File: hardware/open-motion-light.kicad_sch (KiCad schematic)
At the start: 89 parts, among them J1 TYPE-C-31-M-12, J2 Conn_01x04, Q1 2N7002, SW1 SW_Push, SW2 SW_Push, SW3 SSSS213800, U1 CN3058E, U2 STM32L031G6U6, U3 MT9284BS6, U4 PIR223D-S0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

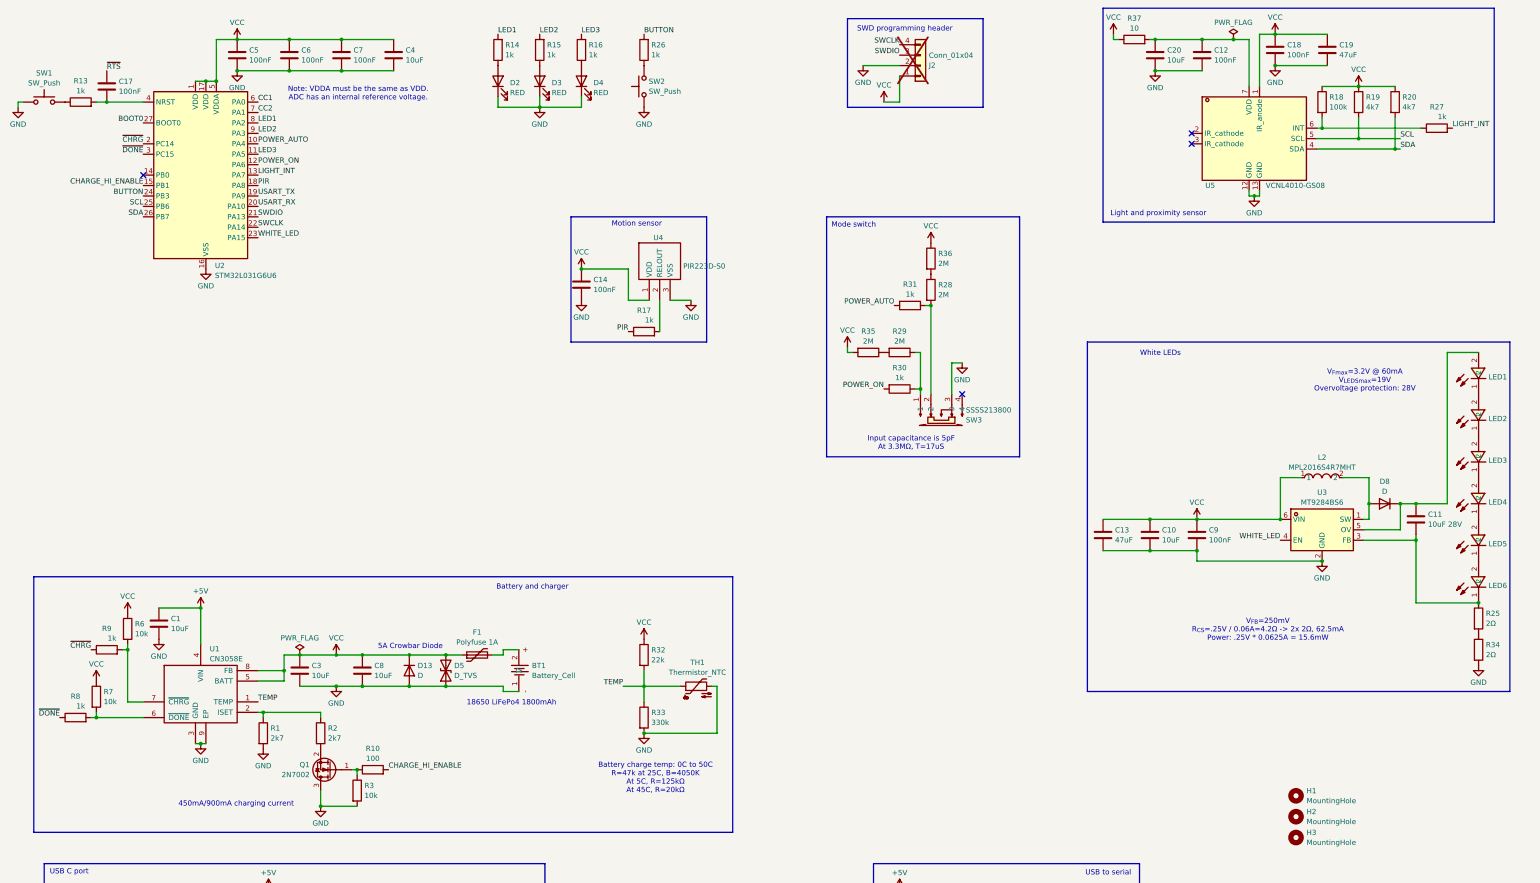
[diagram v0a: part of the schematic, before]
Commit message: Update schematic for v1.1
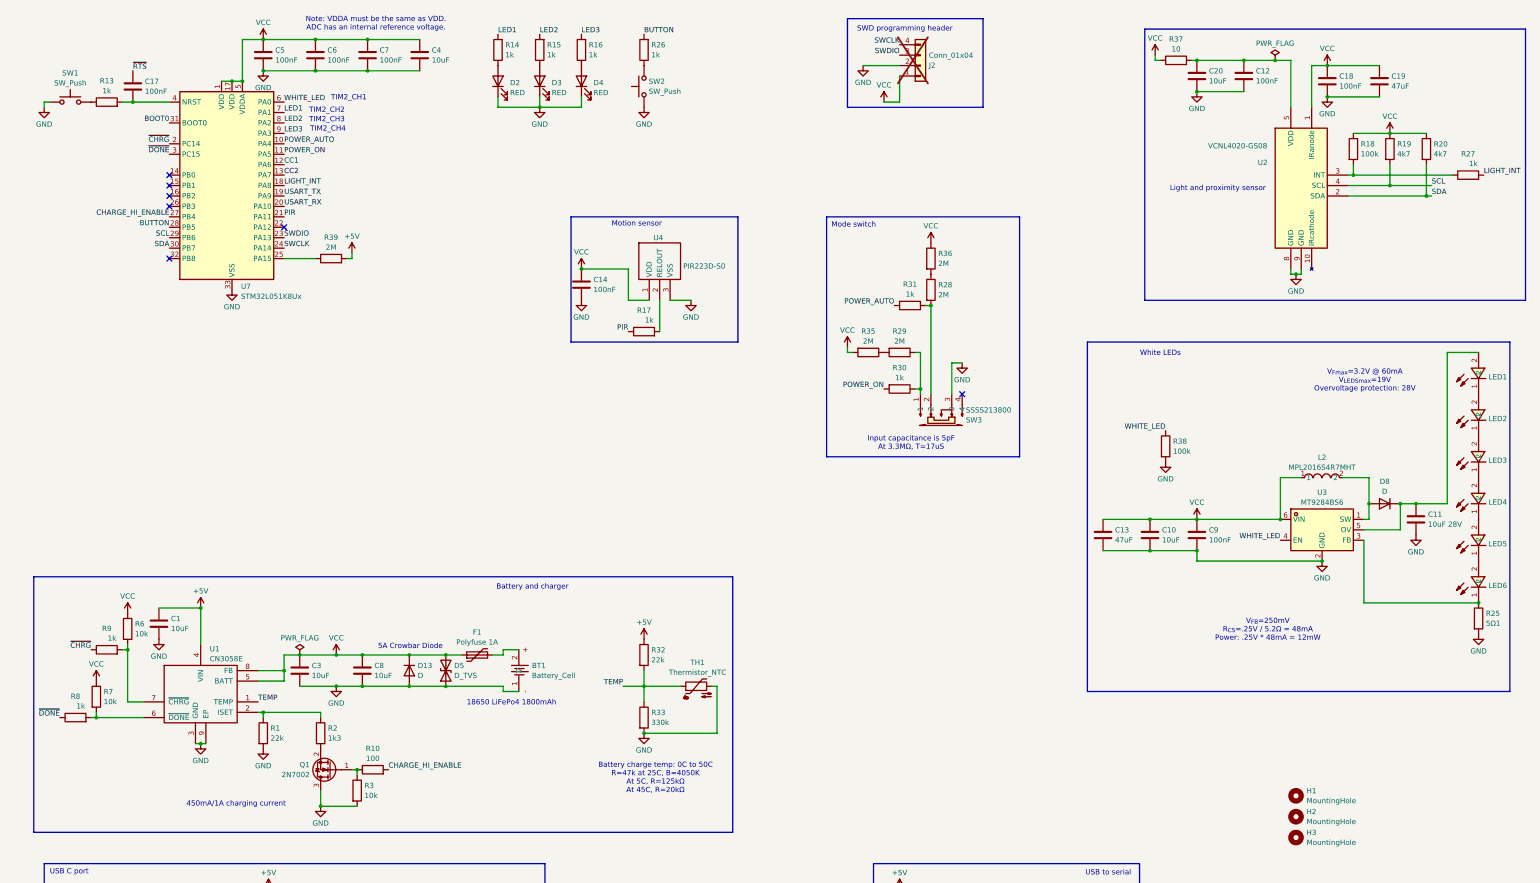
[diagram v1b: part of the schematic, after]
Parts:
- removed R34: 2Ω, Resistor_SMD:R_0603_1608Metric, symbol Device:R
- removed U2: STM32L031G6U6, Package_DFN_QFN:QFN-28_4x4mm_P0.5mm, symbol MCU_ST_STM32L0:STM32L031G6Ux
- removed U5: VCNL4010-GS08, Homebrew:SENSORS-SMD_VCNL4010-GS08, symbol Homebrew:VCNL4010-GS08
- added R38: 100k, Resistor_SMD:R_0402_1005Metric, symbol Device:R
- added R39: 2M, Resistor_SMD:R_0603_1608Metric, symbol Device:R
- added U2: VCNL4020-GS08, Homebrew:SENSOR-SMD_VCNL4020-GS08, symbol Homebrew:VCNL4020-GS08
- added U7: STM32L051K8Ux, Package_DFN_QFN:QFN-32-1EP_5x5mm_P0.5mm_EP3.45x3.45mm, symbol MCU_ST_STM32L0:STM32L051K8Ux
- R1: value 2k7 -> 22k; LCSC C13167 -> (none)
- R2: value 2k7 -> 1k3; LCSC C13167 -> (none)
- R25: value 2Ω -> 5Ω1; LCSC C22977 -> C25197
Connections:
- net +5V: now also R32.1, R39.2
- net BOOT0: now also U7.31 (BOOT0)
- net BUTTON: now also U7.28 (PB5)
- net CC1: now also U7.12 (PA6)
- net CC2: now also U7.13 (PA7)
- net CHARGE_HI_ENABLE: now also U7.27 (PB4)
- net GND: now also C11.2, R25.2, R38.2, U2.8 (GND), U2.9 (GND), U7.33 (VSS)
- net LED1: now also U7.7 (PA1)
- net LED2: now also U7.8 (PA2)
- net LED3: now also U7.9 (PA3)
- net LIGHT_INT: now also U7.18 (PA8)
- net PIR: now also U7.21 (PA11)
- net POWER_AUTO: now also U7.10 (PA4)
- net POWER_ON: now also U7.11 (PA5)
- net SCL: now also U2.4 (SCL), U7.29 (PB6)
- net SDA: now also U2.2 (SDA), U7.30 (PB7)
- net SWCLK: now also U7.24 (PA14)
- net SWDIO: now also U7.23 (PA13)
- net USART_RX: now also U7.20 (PA10)
- net USART_TX: now also U7.19 (PA9)
- net VCC: now also U2.1 (IRanode), U7.1 (VDD), U7.17 (VDD), U7.5 (VDDA); no longer R32.1
- net WHITE_LED: now also R38.1, U7.6 (PA0)
- net ~{CHRG}: now also U7.2 (PC14)
- net ~{DONE}: now also U7.3 (PC15)
- net at C12.2, C20.1, R37.2: now also U2.5 (VDD)
- net at C17.2, R13.2: now also U7.4 (NRST)
- net at R18.2, R27.1: now also U2.3 (INT)
- net at LED6.1, R25.1, U3.3 (FB): no longer C11.2
- new net: R39.1, U7.25 (PA15)
- no-connect marks 8 -> 11
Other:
- note added: "450mA/1A charging current"
- note added: "TIM2_CH1"
- note added: "TIM2_CH2"
- note added: "TIM2_CH3"
- note added: "TIM2_CH4"
- note added: "V_{FB}=250mV R_{CS}=.25V / 5.2Ω = 48mA Power: .25V * 48mA = 12mW"
- note removed: "450mA/900mA charging current"
- note removed: "V_{FB}=250mV R_{CS}=.25V / 0.06A=4.2Ω -> 2x 2Ω, 62.5mA Power: .25V * 0.0625A = 15.6mW"
- moved on the sheet: C12, C17, C18, C19, C20, C4, C5, C6, C7, R13, R18, R19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

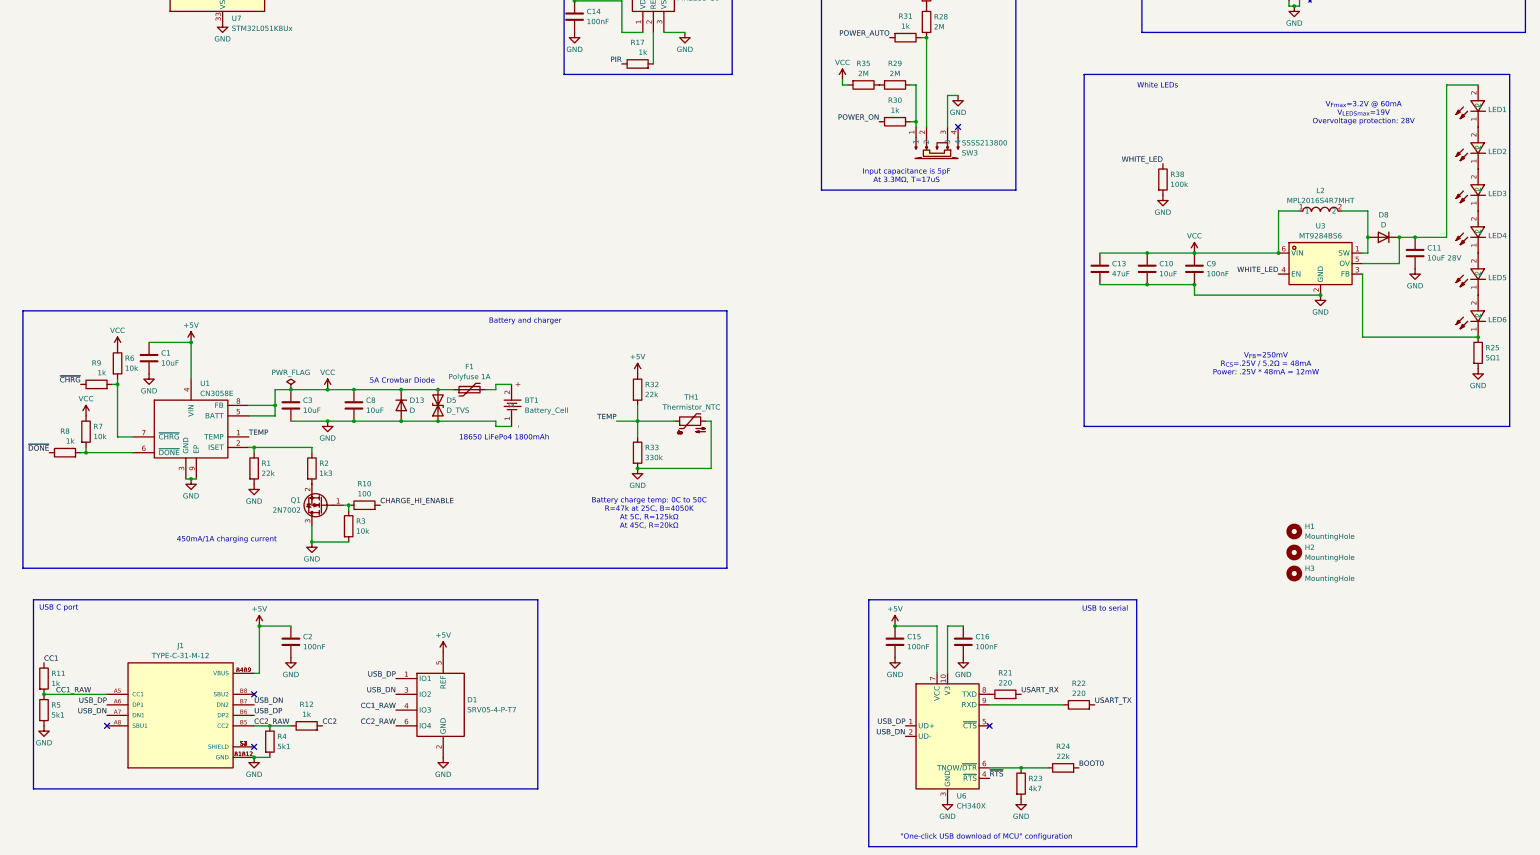
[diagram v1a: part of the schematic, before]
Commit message: More v1.1 schematic updates
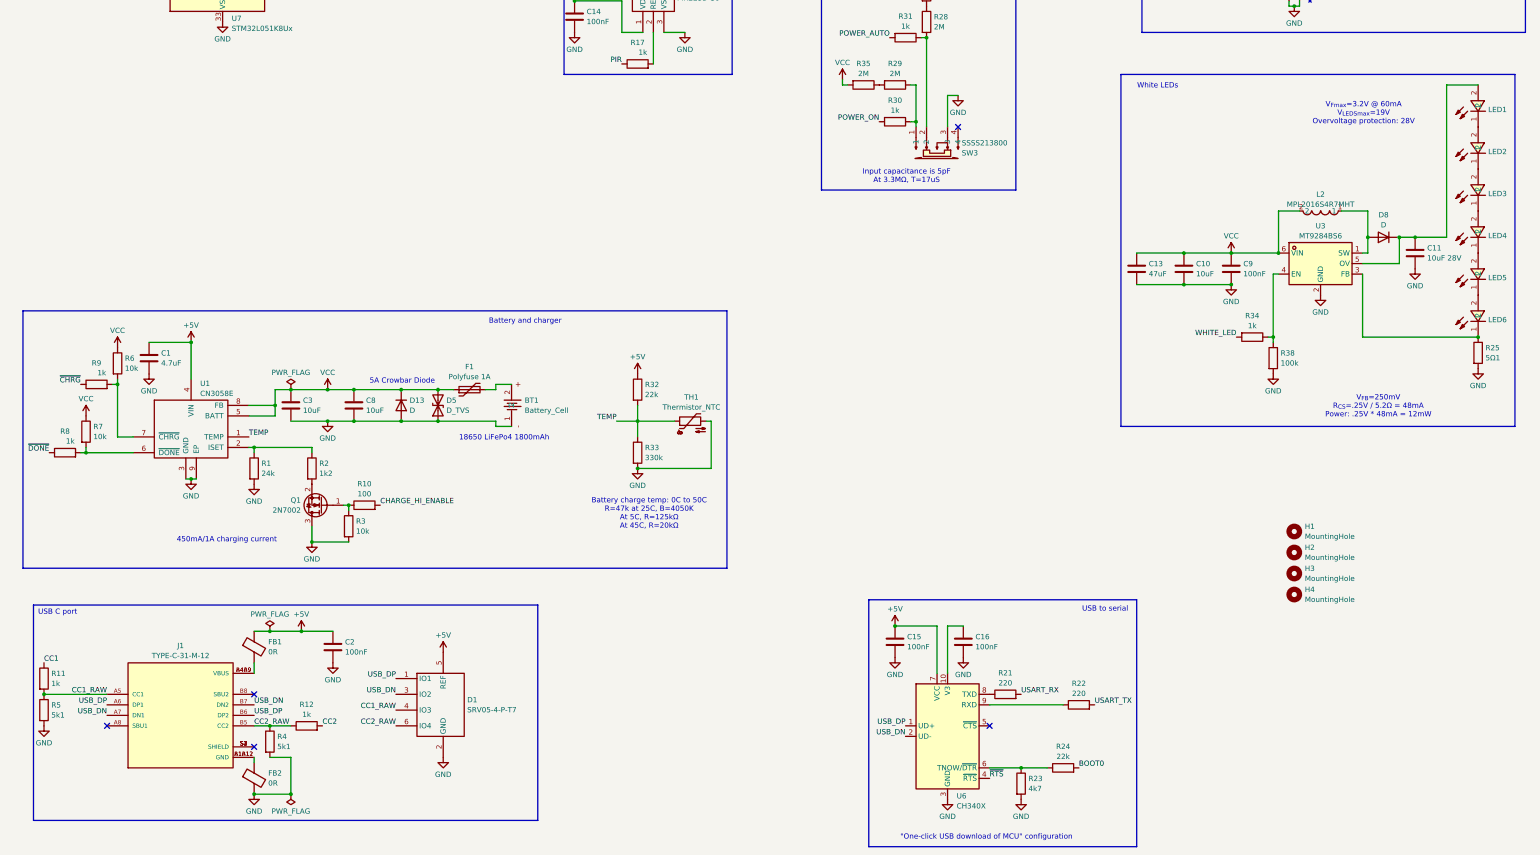
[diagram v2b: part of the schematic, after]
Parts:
- added FB1, FB2: 0R, Inductor_SMD:L_1206_3216Metric, symbol Device:FerriteBead
- added H4: MountingHole, MountingHole:MountingHole_3.2mm_M3_ISO7380, symbol Mechanical:MountingHole
- added R34: 1k, Resistor_SMD:R_0402_1005Metric, symbol Device:R
- C1: value 10uF -> 4.7uF; LCSC C96446 -> C19666
- R1: value 22k -> 24k; LCSC (none) -> C23352
- R2: value 1k3 -> 1k2; LCSC (none) -> 0603
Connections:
- net +5V: now also FB1.1; no longer J1.A4B9 (VBUS), J1.B4A9 (VBUS)
- net GND: now also FB2.2; no longer J1.A1B12 (GND), J1.B1A12 (GND)
- net VCC: now also L2.2; no longer L2.1
- net WHITE_LED: now also R34.2; no longer R38.1, U3.4 (EN)
- net at D8.2 (A), U3.1 (SW): now also L2.1; no longer L2.2
- new net: R34.1, R38.1, U3.4 (EN)
- new net: FB2.1, J1.A1B12 (GND), J1.B1A12 (GND)
- new net: FB1.2, J1.A4B9 (VBUS), J1.B4A9 (VBUS)
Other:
- moved on the sheet: C10, C13, C2, C9, L2, R38

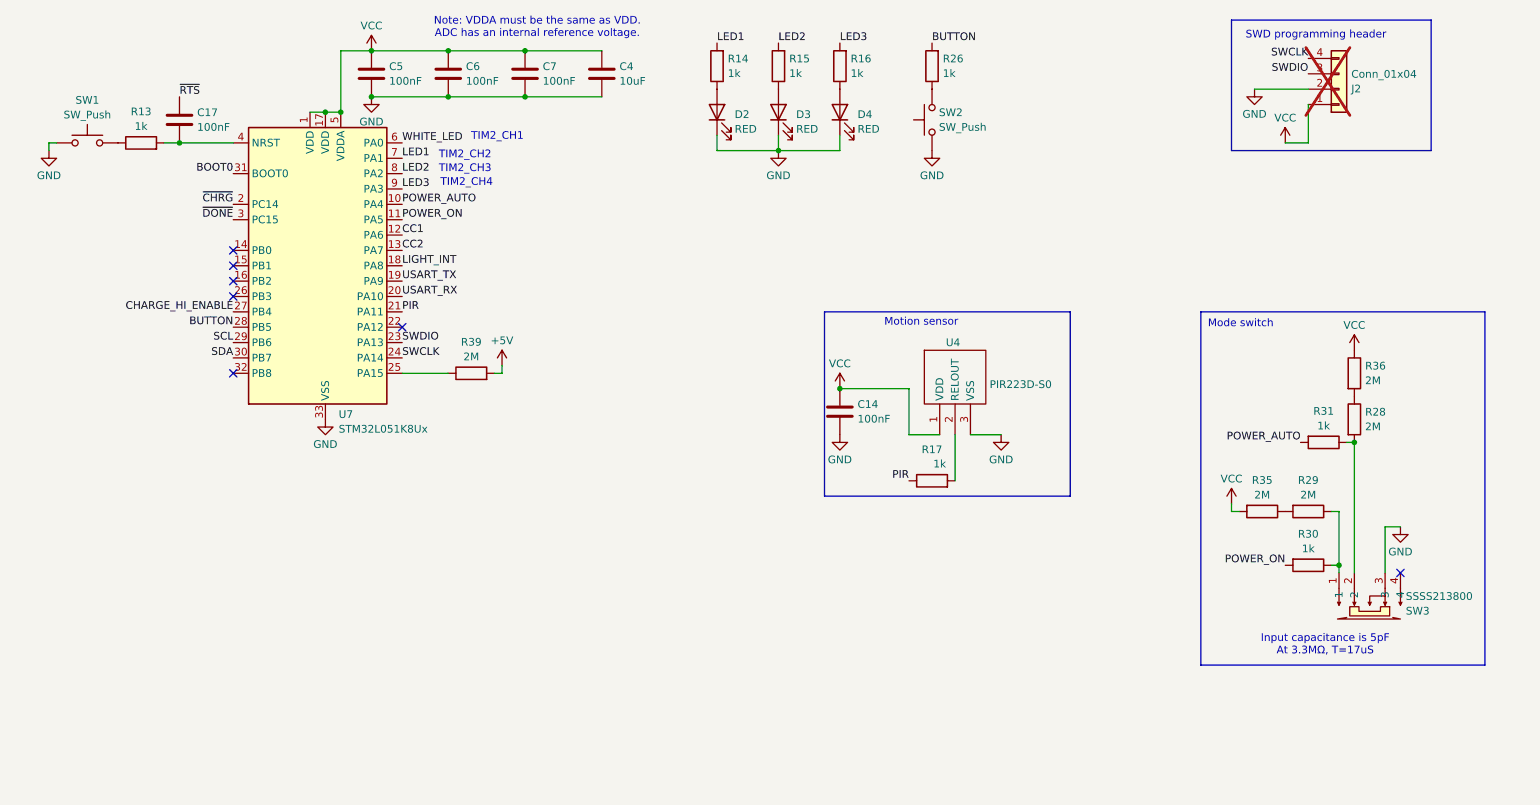
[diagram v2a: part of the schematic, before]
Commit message: Start updating placement and routing for v1.1
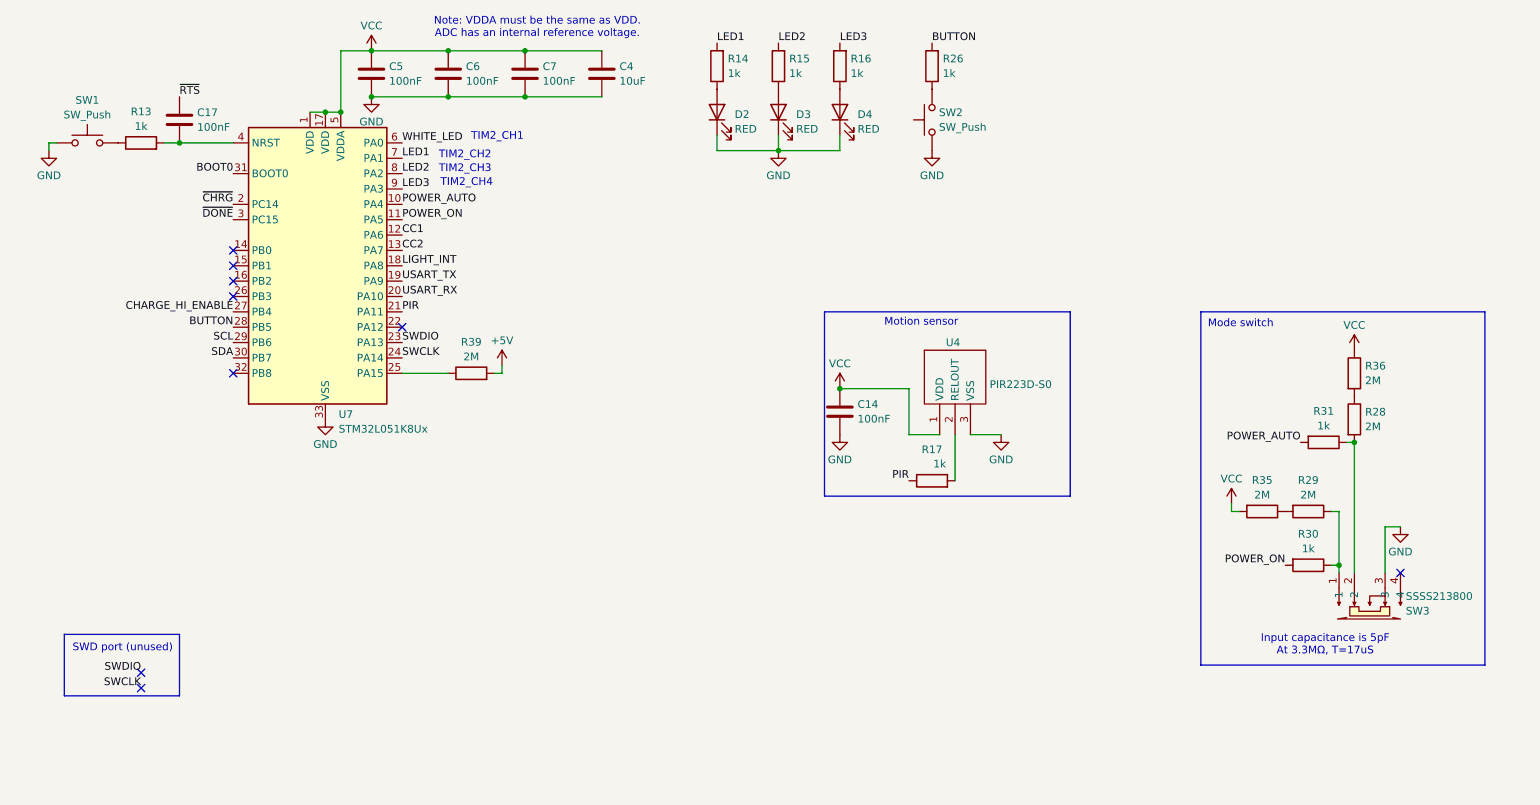
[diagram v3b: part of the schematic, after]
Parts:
- removed J2: Conn_01x04, Connector_PinHeader_2.54mm:PinHeader_1x04_P2.54mm_Vertical, symbol Connector_Generic:Conn_01x04
- U4: footprint Package_TO_SOT_THT:TO-5-3_Window -> Homebrew:PIR223D-S0
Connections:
- no-connect marks 11 -> 13
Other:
- note added: "SWD port (unused)"
- note removed: "SWD programming header"

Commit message: Re-organize schematic
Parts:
- removed R26: 1k, Resistor_SMD:R_0402_1005Metric, symbol Device:R
- removed SW2: SW_Push, Homebrew:SW_TACTILE_5.1MM_TS-1187A-C-D-B, symbol Switch:SW_Push
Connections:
- net BUTTON: no longer names the net of U7.28 (PB5)
- net SWCLK: no longer names the net of U7.24 (PA14)
- net SWDIO: no longer names the net of U7.23 (PA13)
- no-connect marks 13 -> 14
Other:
- note added: "Battery indicator LEDs"
- note added: "MCU"
- note removed: "SWD port (unused)"
- moved on the sheet: BT1, C1, C10, C11, C12, C13, C14, C15, C16, C17, C18, C19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

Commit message: Update PCB for circle layout
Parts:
- removed D5: D_TVS, Diode_SMD:D_0402_1005Metric, symbol Device:D_TVS
- removed H4: MountingHole, MountingHole:MountingHole_3.2mm_M3_ISO7380, symbol Mechanical:MountingHole
- removed R17: 1k, Resistor_SMD:R_0402_1005Metric, symbol Device:R
- added D5, D6, D7, D9: ESD5Z5.0, Diode_SMD:D_SOD-523, symbol Diode:ESD5Zxx
- added R26: 10k, Resistor_SMD:R_0402_1005Metric, symbol Device:R
- F1: value Polyfuse 1A -> BSMD1206-100-6V
- R2: value 1k2 -> 1k5; LCSC 0603 -> C22843
- R30, R31: value 1k -> 10k; LCSC C11702 -> C25744
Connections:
- net GND: now also D5.2 (A), D6.2 (A), D7.2 (A), D9.2 (A)
- net PIR: now also R26.2
- net USB_DN: now also D1.1 (IO1); no longer D1.3 (IO2)
- net USB_DP: now also D1.3 (IO2); no longer D1.1 (IO1)
- net VCC: now also D6.1 (K)
- net at R28.2, R31.1, SW3.2: now also D5.1 (K)
- net at R29.1, R30.1, SW3.1: now also D7.1 (K)
- net at U4.2 (RELOUT): now also D9.1 (K), R26.1
- net at FB2.1, J1.A1B12 (GND), J1.B1A12 (GND): now also J1.S1 (SHIELD), J1.S2 (SHIELD), J1.S3 (SHIELD), J1.S4 (SHIELD)
- no-connect marks 14 -> 13
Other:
- note added: "1A Polyfuse"
- note added: "450mA/900mA charging current"
- note added: "MCU input capacitance is 5pF At 4MΩ, T=20us"
- note added: "TODO: connect shield?"
- note removed: "450mA/1A charging current"
- note removed: "Input capacitance is 5pF At 3.3MΩ, T=17uS"
- moved on the sheet: R28, R29, R30, R31, R35, R36, SW3
